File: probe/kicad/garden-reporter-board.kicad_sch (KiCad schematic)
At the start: 21 parts, among them J1 70543-0106, J2 Conn_01x02, J3 70543-0002, J4 70543-0002, J5 70543-0002, Q1 TN0702N3-G, U1 MCP1700-3302E_TO92, U2 MCP1700-3302E_TO92

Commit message: Feature/v divider for sensors
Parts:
- added R3: 10K 1%, Resistor_THT:R_Axial_DIN0207_L6.3mm_D2.5mm_P7.62mm_Horizontal, symbol Device:R_Small
- added R4: 5K 1%, Resistor_THT:R_Axial_DIN0207_L6.3mm_D2.5mm_P7.62mm_Horizontal, symbol Device:R_Small
- J5: footprint Connector_Molex:Molex_SL_171971-0003_1x03_P2.54mm_Vertical -> Connector_Molex:Molex_SL_171971-0002_1x02_P2.54mm_Vertical; symbol Connector_Generic:Conn_01x03 -> Connector_Generic:Conn_01x02
- R2: value 10K 1% -> 2K 1%
- R5: renamed from R3; value 10K 1% -> 180 1%
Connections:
- net GND1: now also R4.2; no longer J5.3 (Pin_3)
- net sensor_soil: now also R3.2, R4.1; no longer J3.2 (Pin_2)
- new net: J3.2 (Pin_2), R3.1
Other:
- note added: "Capacitor sensor for soil moisture --> Use DFRobot coz it's documented 426-SEN0193 Requires calibration, to get value range [dry; water] Requires mechanical protection to last, considering epoxy coating V Divider 1/3 so range [0 - 1.1V] is below ADC max (1.2V)"
- note added: "TEPT5700 Read Voltage, with U=RI I=U/R Use datasheet to translate I to DegC --> Keep R lowest possible ? so that can measure higher I values ... ie higher lux values ? --> Max Ice = 20mA so aim for 18mA 3.3V / 0.018A = 183 Ohm Use 180"
- note added: "TMP36GT9Z Add 1uF next to body, ie on wire 750mV at 25degC, 10mV per degC ADC saturates at 1.2V -> 70deg Use thermally conductive epox on ic"
- note added: "Use V-divider x1/6 with zener diode to ensure line is <= 3.3V R 1/4W 1% metal film, could be: - 603-MFR-25FRF5210K - 603-MFR-25FRF5202K"
- note removed: "Capacitor sensor for soil moisture --> Use DFRobot coz it's documented 426-SEN0193 Requires calibration, to get value range [dry; water] Requires mechanical protection to last, considering epoxy coating"
- note removed: "TEPT5700 Read Voltage, with U=RI I=U/R Use datasheet to translate I to DegC - it depends on VCC too !"
- note removed: "TMP36GT9Z Add 1uF next to body, ie on wire 750mV at 25degC, 10mV per degC Use thermally conductive epox on ic"
- note removed: "Use V-divider x1/2 with zener diode to ensure line is <= 3.3V R 1/4W 1% metal film, could be: - 603-MFR-25FRF5210K Note: divider could be more adjusted but good enough with 10K, which keep the BOM small"
- moved on the sheet: R5

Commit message: TODOs and docs on V-divider for light sensor
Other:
- note added: "TEPT5700 with MCP1700-1202 (1.2V reg) Read Voltage, with U=RI I=U/R Use datasheet to translate I to DegC --> Keep R lowest possible ? so that can measure higher I values ... ie higher lux values ? --> Max Ice = 20mA so aim for 18mA 1.2V / 0.018A = 66.6667 Ohm Use 65"
- note added: "TMP36GT9Z (can use LM61BIZ) Add 1uF next to body, ie on wire 750mV at 25degC, 10mV per degC ADC saturates at 1.2V -> 70deg Use thermally conductive epox on ic"
- note added: "TODO better attchment of PCB"
- note removed: "TEPT5700 Read Voltage, with U=RI I=U/R Use datasheet to translate I to DegC --> Keep R lowest possible ? so that can measure higher I values ... ie higher lux values ? --> Max Ice = 20mA so aim for 18mA 3.3V / 0.018A = 183 Ohm Use 180"
- note removed: "TMP36GT9Z Add 1uF next to body, ie on wire 750mV at 25degC, 10mV per degC ADC saturates at 1.2V -> 70deg Use thermally conductive epox on ic"
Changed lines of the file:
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@@
+    (effects (font (size 1.27 1.27)) (justify left bottom))
+  )
+  (text "TODO better attchment of PCB" (at 165.1 119.38 0)
     (effects (font (size 1.27 1.27)) (justify left bottom))
   )
@@
     (effects (font (size 1.27 1.27)) (justify left bottom))
   )
-  (text "TMP36GT9Z\nAdd 1uF next to body, ie on wire\n750mV at 25degC, 10mV per degC\nADC saturates at 1.2V -> 70deg\nUse thermally conductive epox on ic"
+  (text "TMP36GT9Z (can use LM61BIZ)\nAdd 1uF next to body, ie on wire\n750mV at 25degC, 10mV per degC\nADC saturates at 1.2V -> 70deg\nUse thermally conductive epox on ic"
     (at 210.82 100.33 0)
     (effects (font (size 1.27 1.27)) (justify left bottom))
@@
     (effects (font (size 1.27 1.27)) (justify left bottom))
   )
-  (text "TEPT5700\nRead Voltage, with U=RI I=U/R\nUse datasheet to translate I to DegC\n--> Keep R lowest possible ?\n    so that can measure higher I values\n    ... ie higher lux values ?\n--> Max Ice = 20mA so aim for 18mA\n    3.3V / 0.018A = 183 Ohm\n    Use 180"
+  (text "TEPT5700 with MCP1700-1202 (1.2V reg)\nRead Voltage, with U=RI I=U/R\nUse datasheet to translate I to DegC\n--> Keep R lowest possible ?\n    so that can measure higher I values\n    ... ie higher lux values ?\n--> Max Ice = 20mA so aim for 18mA\n    1.2V / 0.018A = 66.6667 Ohm\n    Use 65"
     (at 186.69 163.83 0)
     (effects (font (size 1.27 1.27)) (justify left bottom))

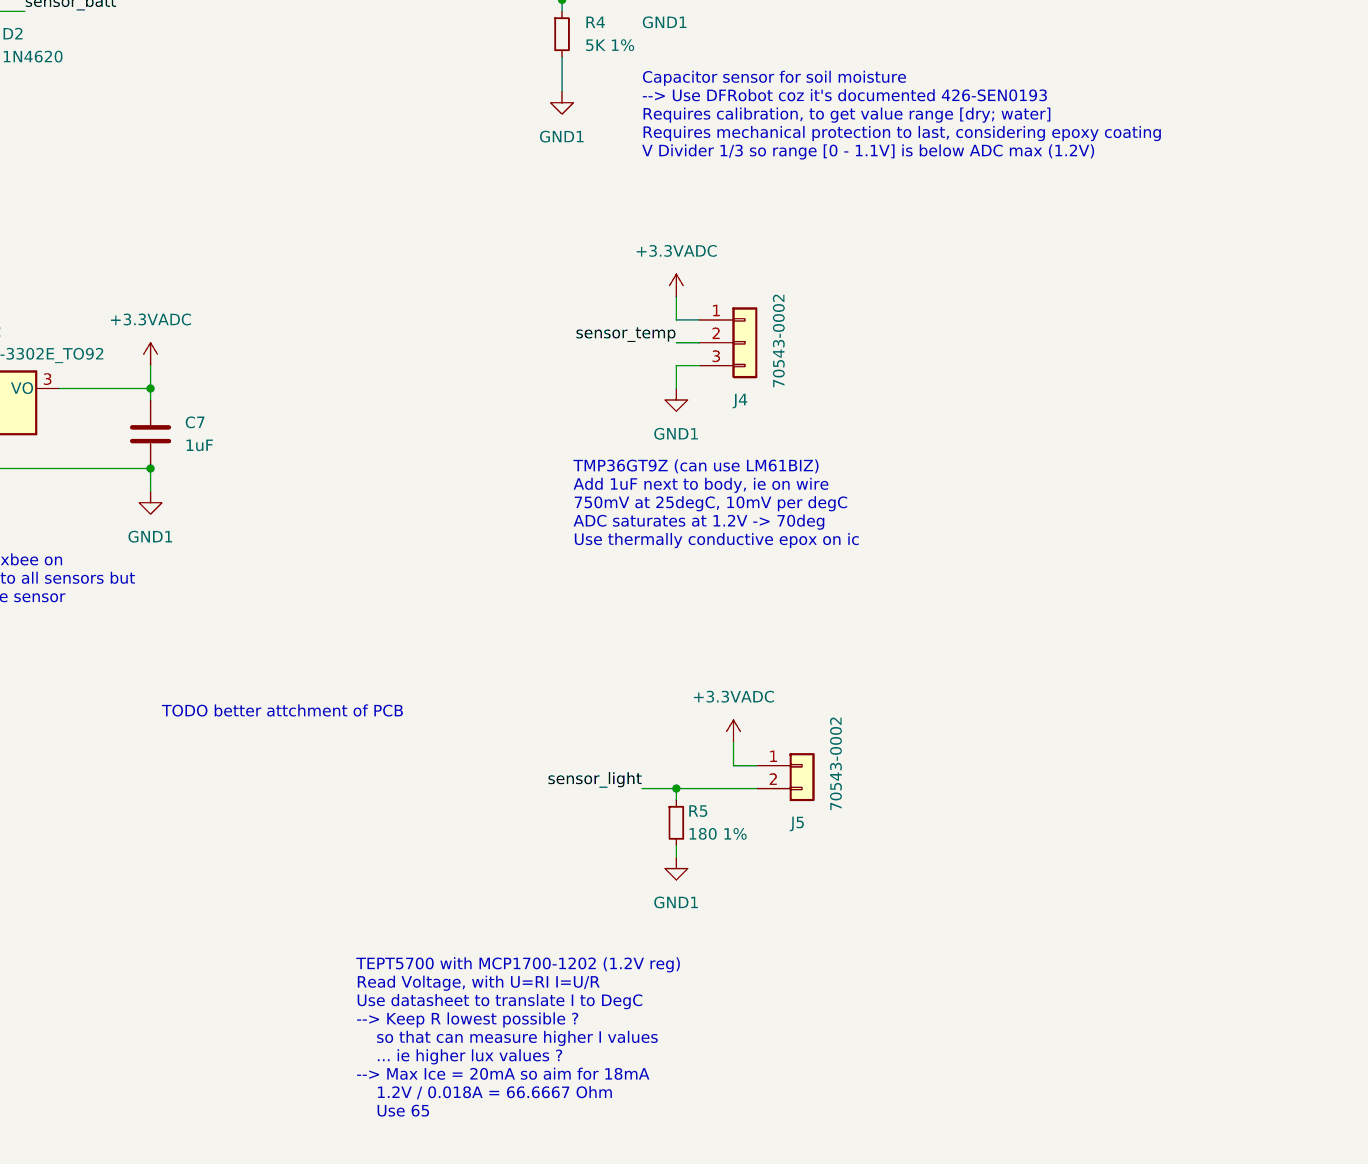
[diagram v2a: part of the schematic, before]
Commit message: Add to light sensor V reg to 1.2V, adjust light R properly, fix layout accordingly
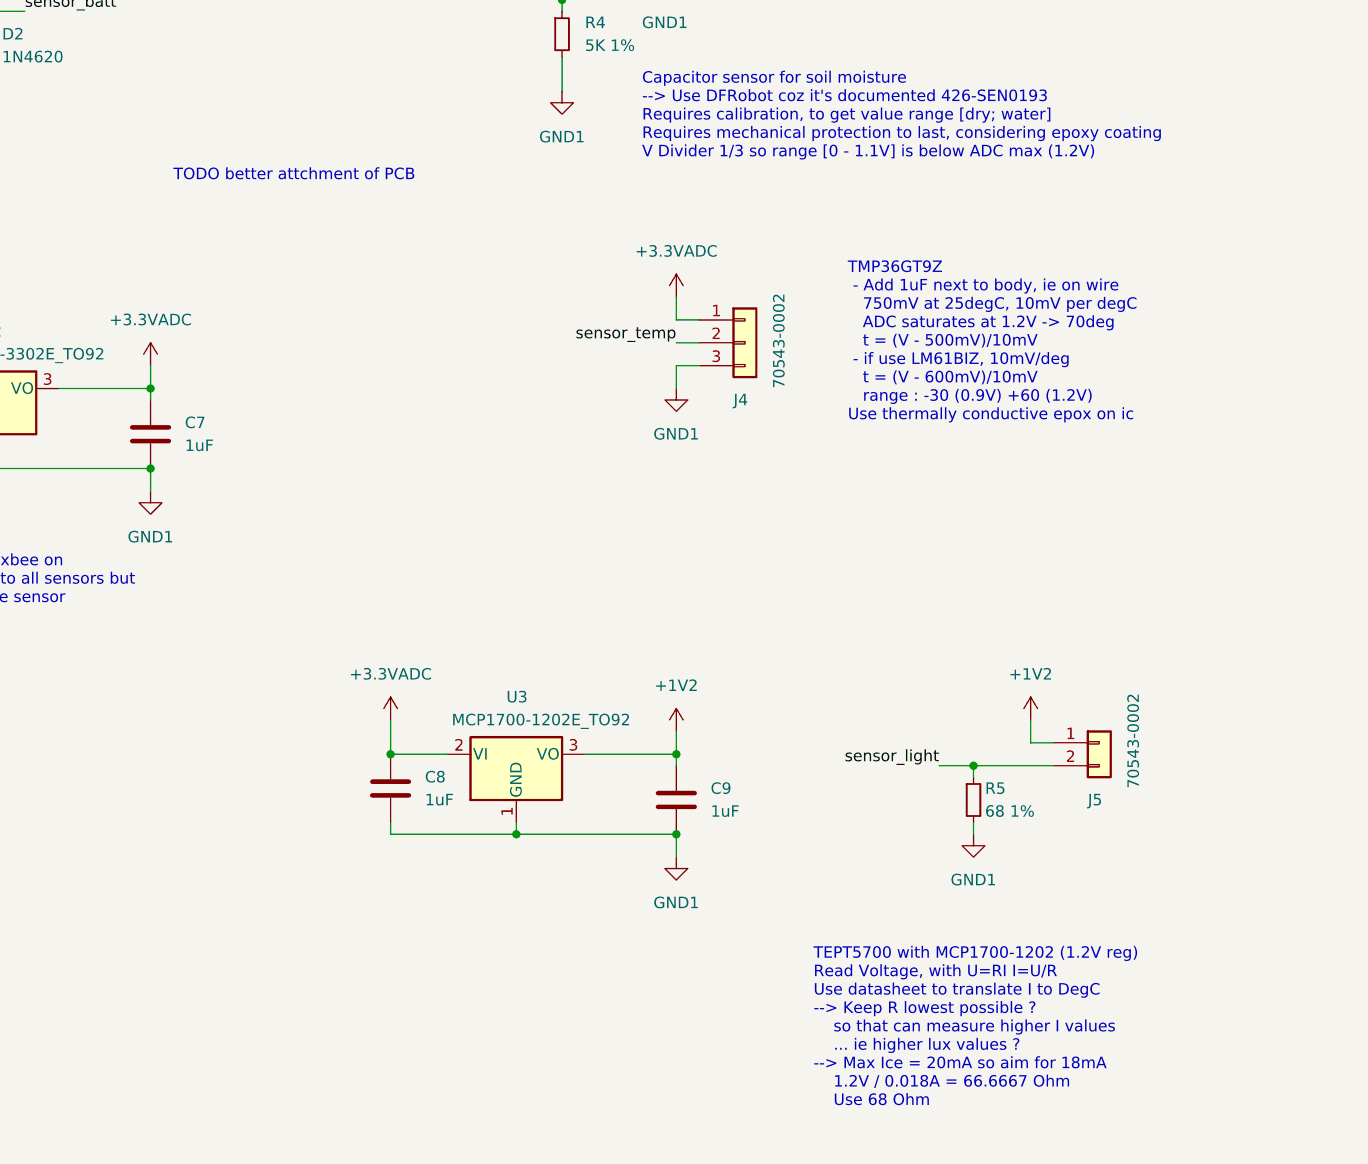
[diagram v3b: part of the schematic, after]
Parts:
- added C8, C9: 1uF, Capacitor_THT:C_Disc_D3.0mm_W2.0mm_P2.50mm, symbol Device:C
- added U3: MCP1700-1202E_TO92, Package_TO_SOT_THT:TO-92_Inline, symbol Regulator_Linear:MCP1700-3302E_TO92
- R5: value 180 1% -> 68 1%
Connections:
- net +3.3VADC: now also C8.1, U3.2 (VI); no longer J5.1 (Pin_1)
- net GND1: now also C8.2, C9.2, U3.1 (GND)
- new net +1V2: C9.1, J5.1 (Pin_1), U3.3 (VO)
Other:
- note added: "TEPT5700 with MCP1700-1202 (1.2V reg) Read Voltage, with U=RI I=U/R Use datasheet to translate I to DegC --> Keep R lowest possible ? so that can measure higher I values ... ie higher lux values ? --> Max Ice = 20mA so aim for 18mA 1.2V / 0.018A = 66.6667 Ohm Use 68 Ohm"
- note added: "TMP36GT9Z - Add 1uF next to body, ie on wire 750mV at 25degC, 10mV per degC ADC saturates at 1.2V -> 70deg t = (V - 500mV)/10mV - if use LM61BIZ, 10mV/deg t = (V - 600mV)/10mV range : -30 (0.9V) +60 (1.2V) Use thermally conductive epox on ic"
- note removed: "TEPT5700 with MCP1700-1202 (1.2V reg) Read Voltage, with U=RI I=U/R Use datasheet to translate I to DegC --> Keep R lowest possible ? so that can measure higher I values ... ie higher lux values ? --> Max Ice = 20mA so aim for 18mA 1.2V / 0.018A = 66.6667 Ohm Use 65"
- note removed: "TMP36GT9Z (can use LM61BIZ) Add 1uF next to body, ie on wire 750mV at 25degC, 10mV per degC ADC saturates at 1.2V -> 70deg Use thermally conductive epox on ic"
- moved on the sheet: J5, R5

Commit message: Comment on soil moisture sensor and V-divider
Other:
- note added: "TODO V-divider no work ! I remember that I had to put the tripot to an edge There's something about a single R being enough coz there's already an R on sensor board"
- note removed: "TODO better attchment of PCB"
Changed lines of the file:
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@@
     (effects (font (size 1.27 1.27)) (justify left bottom))
   )
-  (text "TODO better attchment of PCB" (at 166.37 59.69 0)
+  (text "TODO V-divider no work !\n  I remember that I had to put the tripot to an edge\n  There's something about a single R being enough \n  coz there's already an R on sensor board"
+    (at 228.6 20.32 0)
     (effects (font (size 1.27 1.27)) (justify left bottom))
   )
